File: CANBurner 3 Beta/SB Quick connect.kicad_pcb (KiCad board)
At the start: 2 copper layers, 33.8 x 30 mm, 9 parts

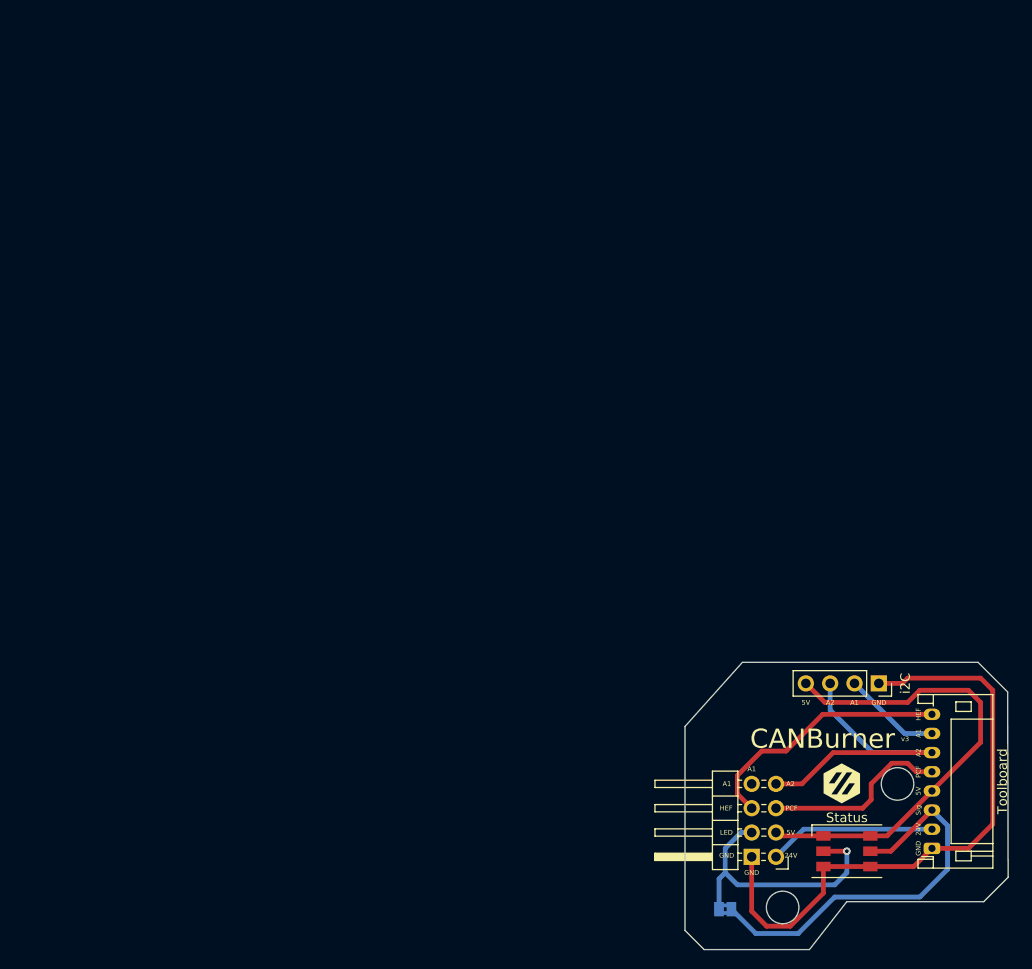
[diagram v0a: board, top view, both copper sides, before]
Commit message: Modified pin order on i2c header
Now fits better with the order most breakouts use.
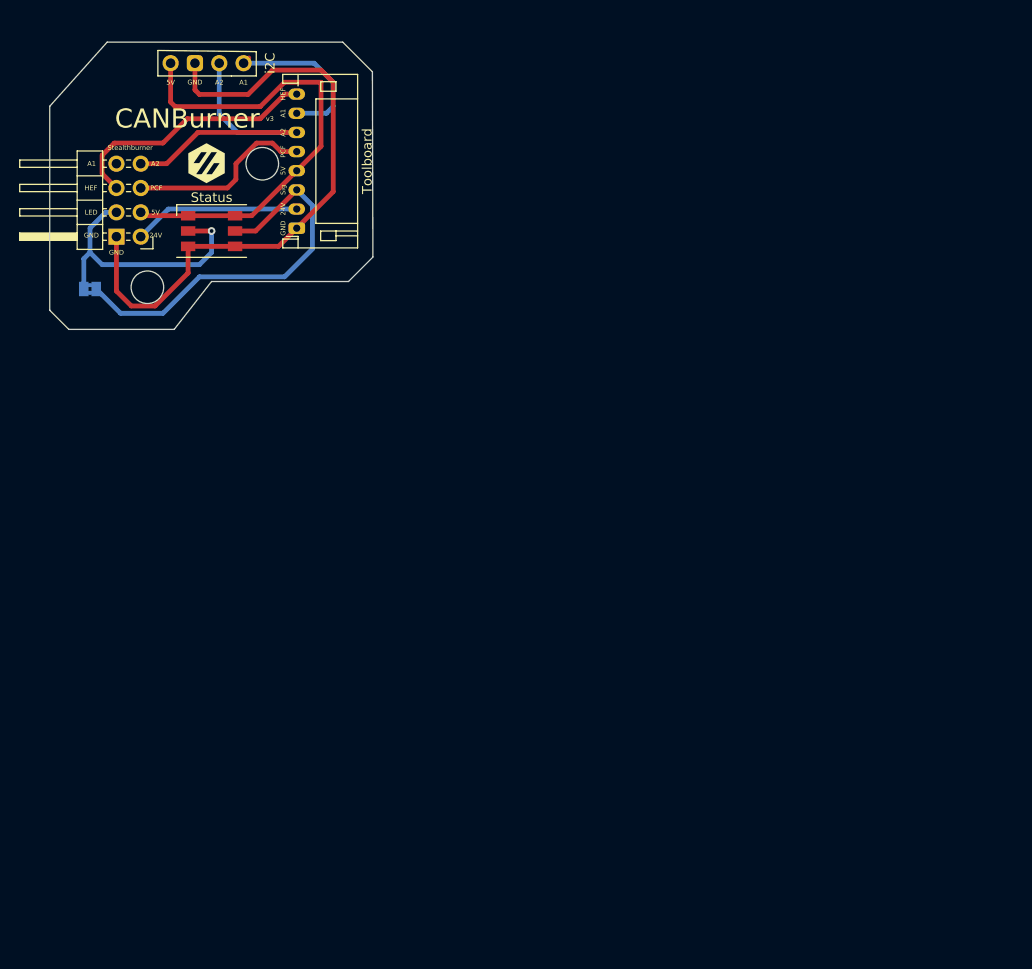
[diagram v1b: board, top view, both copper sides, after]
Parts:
- moved G*** 92.7 mm to (59.4, 29.2)
- moved LED Bypass 92.7 mm to (59.4, 48.3)
- moved Status 92.7 mm to (72.1, 42.2)
- moved G*** 92.7 mm to (71.6, 35.1) (x2)
- moved G*** 92.7 mm to (61.9, 26.7)
- moved Stealthburner 92.7 mm to (54.1, 35.2)
- moved Toolboard 92.7 mm to (81.0, 41.9)
- moved i2C 92.7 mm to (75.4, 24.7)
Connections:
- i2C pad 1: /GND -> /A1
- i2C pad 2: /A1 -> /A2
- i2C pad 3: /A2 -> /GND
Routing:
- net /A1: track 10.3 -> 17.6 mm
- net /A2: track 32.9 -> 31.8 mm
- net /GND: track 65.0 -> 66.0 mm
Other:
- outline, holes or cut-outs redrawn

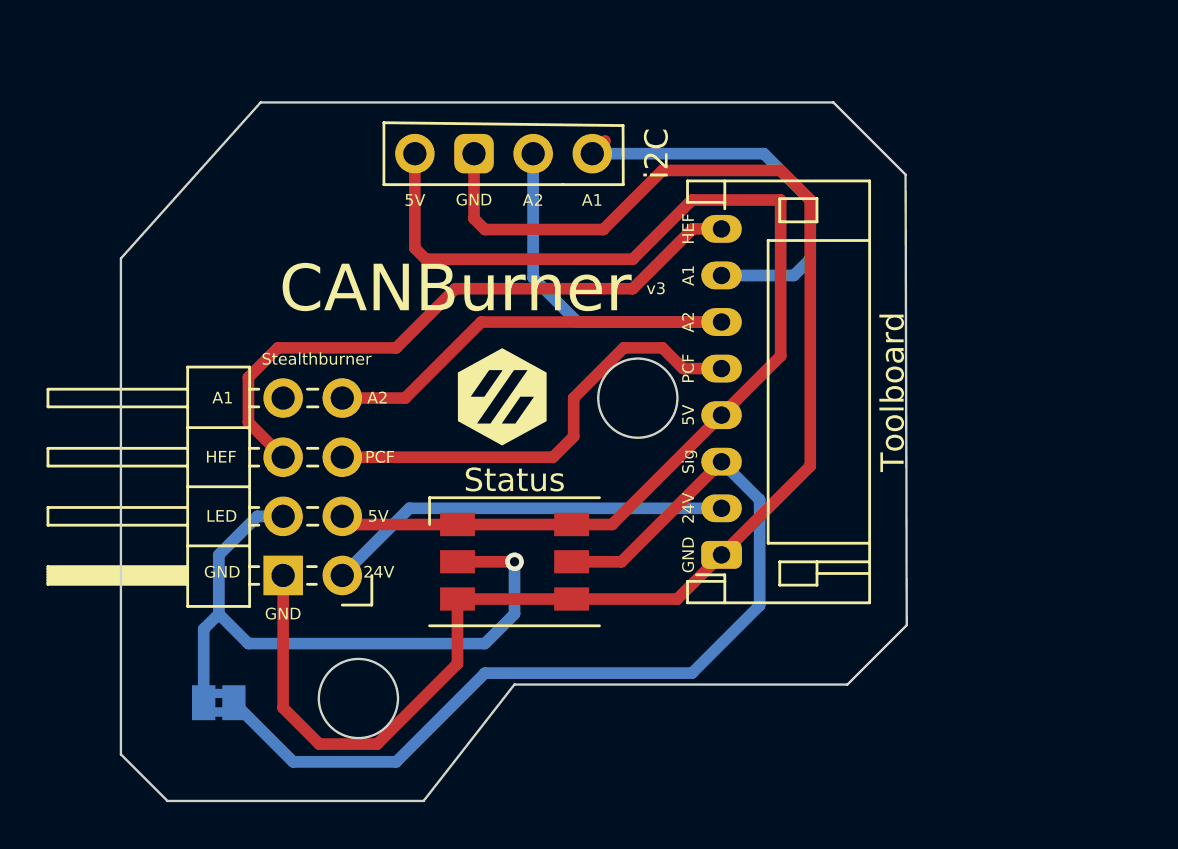
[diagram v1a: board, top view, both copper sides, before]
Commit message: Minor adjustments to LED Signal tracks
Moved tracks further from edges/mounting screws
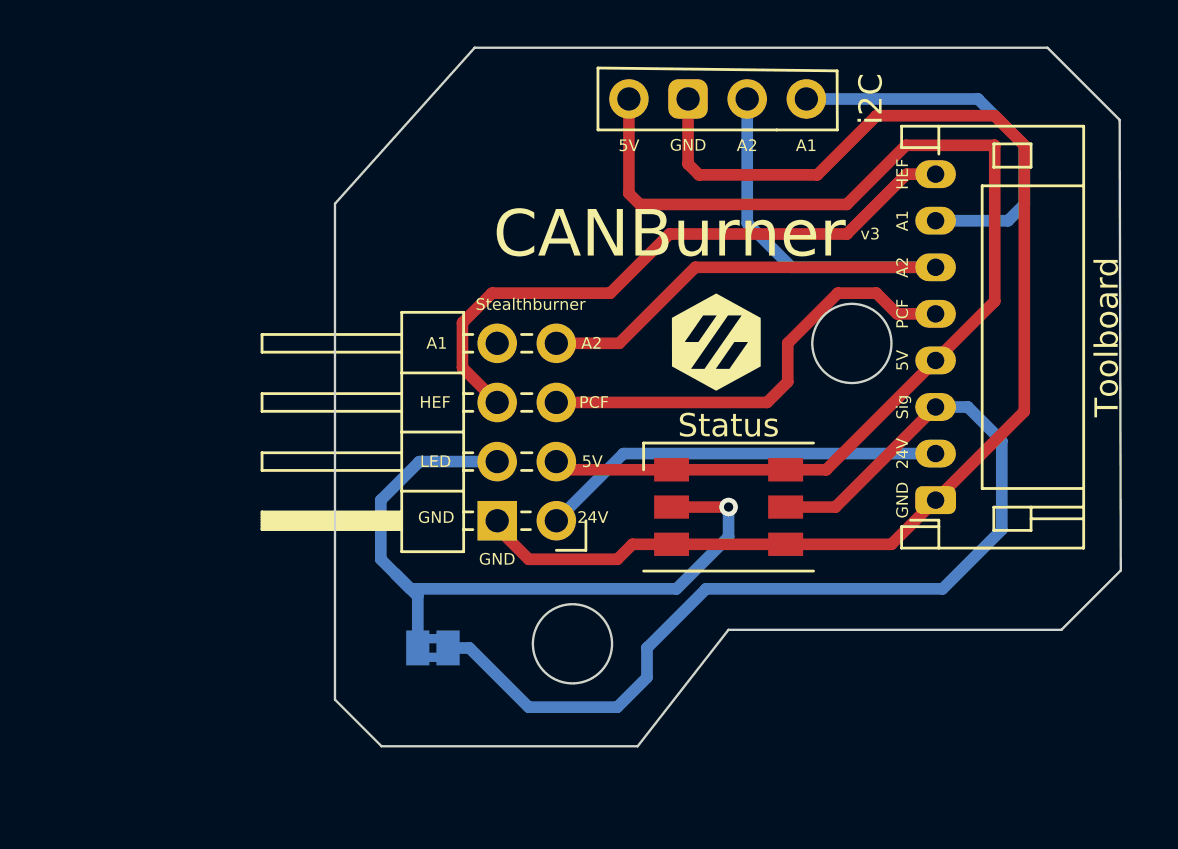
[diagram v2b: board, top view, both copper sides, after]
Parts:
- moved G*** 9.49 mm to (68.6, 26.9)
- moved G*** 9.49 mm to (80.8, 32.7) (x2)
- moved G*** 9.49 mm to (71.1, 24.3)
- moved LED Bypass 9.49 mm to (68.6, 45.9)
- moved Status 9.49 mm to (81.3, 39.9)
- moved Stealthburner 9.49 mm to (63.3, 32.8)
- moved Toolboard 9.49 mm to (90.2, 39.6)
- moved i2C 9.49 mm to (84.6, 22.3)
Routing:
- net /GND: track 66.0 -> 56.6 mm
- net /Sig: track 70.0 -> 76.1 mm
- net /A1: track 17.6 -> 16.8 mm

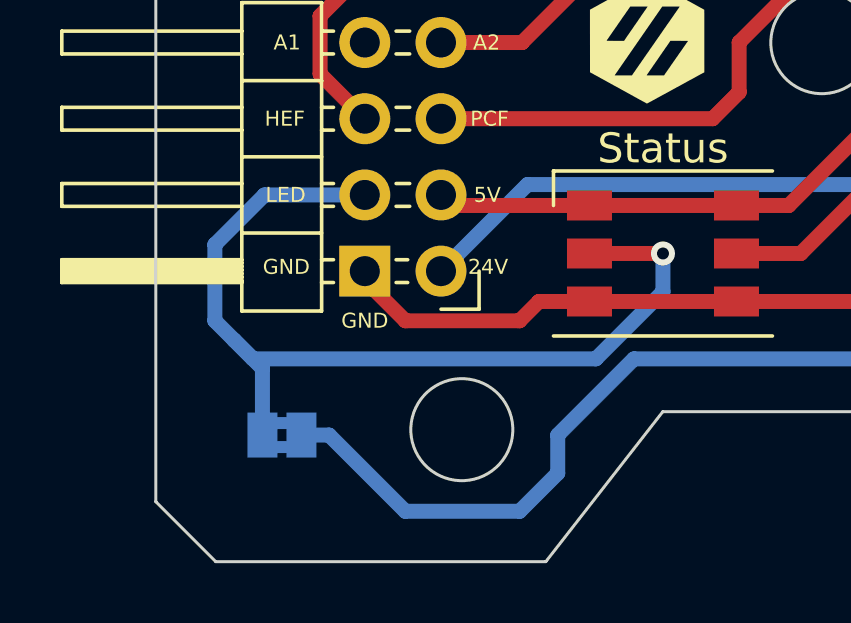
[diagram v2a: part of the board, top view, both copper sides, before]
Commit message: Another LED Signal Track tweak
Slightly adjusted the tracks on the bypass pad
so the path is more obvious when looking at tracks on printed board
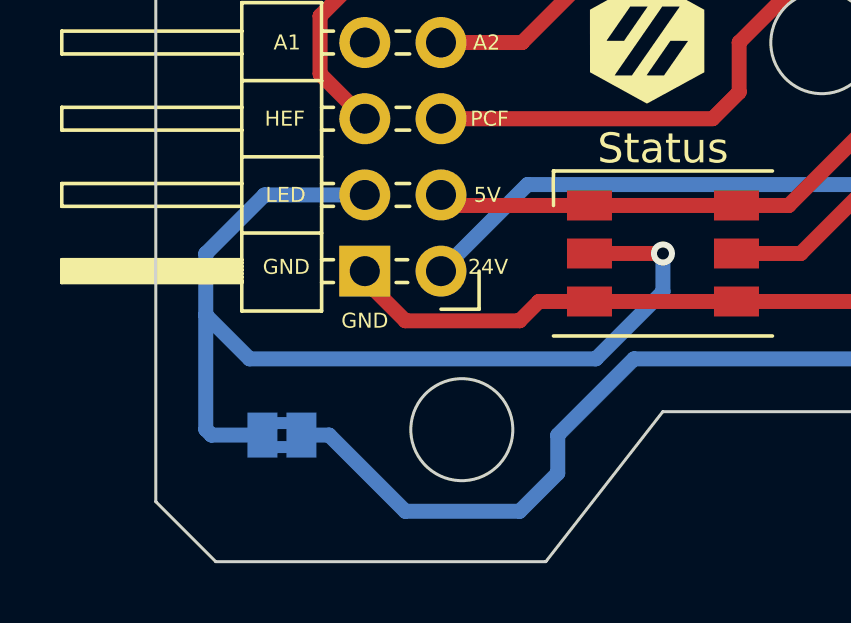
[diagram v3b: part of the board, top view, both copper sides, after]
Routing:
- net /Sig: track 76.1 -> 78.6 mm
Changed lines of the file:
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@@
   (segment (start 85.873186 39.856814) (end 83.73 39.856814) (width 0.5) (layer "F.Cu") (net 6))
   (via blind (at 81.28 39.856814) (size 0.8) (drill 0.4) (layers "F.Cu" "B.Cu") (free) (net 6))
-  (segment (start 81.28 39.856814) (end 81.28 41.133145) (width 0.5) (layer "B.Cu") (net 6))
   (segment (start 81.28 41.133145) (end 79.043145 43.37) (width 0.5) (layer "B.Cu") (net 6))
   (segment (start 93.013145 37.02) (end 93.013145 40.83) (width 0.5) (layer "B.Cu") (net 6))
   (segment (start 77.773145 45.91) (end 77.773145 47.18) (width 0.5) (layer "B.Cu") (net 6))
-  (segment (start 66.343145 42.1) (end 66.343145 39.56) (width 0.5) (layer "B.Cu") (net 6))
-  (segment (start 66.978145 42.735) (end 66.343145 42.1) (width 0.5) (layer "B.Cu") (net 6))
   (segment (start 91.553145 35.56) (end 93.013145 37.02) (width 0.5) (layer "B.Cu") (net 6))
-  (segment (start 67.93 45.91) (end 67.93 43.686855) (width 0.5) (layer "B.Cu") (net 6))
+  (segment (start 67.998119 37.905026) (end 71.341315 37.905026) (width 0.5) (layer "B.Cu") (net 6))
+  (segment (start 66.04 41.91) (end 66.04 39.863145) (width 0.5) (layer "B.Cu") (net 6))
   (segment (start 90.473145 43.37) (end 80.313145 43.37) (width 0.5) (layer "B.Cu") (net 6))
   (segment (start 90.17 35.56) (end 91.553145 35.56) (width 0.5) (layer "B.Cu") (net 6))
-  (segment (start 67.613145 43.37) (end 66.978145 42.735) (width 0.5) (layer "B.Cu") (net 6))
+  (segment (start 81.28 39.856814) (end 81.28 41.133145) (width 0.5) (layer "B.Cu") (net 6))
+  (segment (start 66.04 41.91) (end 66.04 45.72) (width 0.5) (layer "B.Cu") (net 6))
   (segment (start 70.153145 45.91) (end 69.23 45.91) (width 0.5) (layer "B.Cu") (net 6))
   (segment (start 72.693145 48.45) (end 70.153145 45.91) (width 0.5) (layer "B.Cu") (net 6))
   (segment (start 77.773145 47.18) (end 76.503145 48.45) (width 0.5) (layer "B.Cu") (net 6))
+  (segment (start 66.04 45.72) (end 66.23 45.91) (width 0.5) (layer "B.Cu") (net 6))
   (segment (start 93.013145 40.83) (end 90.473145 43.37) (width 0.5) (layer "B.Cu") (net 6))
   (segment (start 76.503145 48.45) (end 72.693145 48.45) (width 0.5) (layer "B.Cu") (net 6))
-  (segment (start 66.343145 39.56) (end 67.998119 37.905026) (width 0.5) (layer "B.Cu") (net 6))
-  (segment (start 67.998119 37.905026) (end 71.341315 37.905026) (width 0.5) (layer "B.Cu") (net 6))
+  (segment (start 67.5 43.37) (end 66.04 41.91) (width 0.5) (layer "B.Cu") (net 6))
   (segment (start 80.313145 43.37) (end 77.773145 45.91) (width 0.5) (layer "B.Cu") (net 6))
-  (segment (start 67.93 43.686855) (end 66.978145 42.735) (width 0.5) (layer "B.Cu") (net 6))
-  (segment (start 79.043145 43.37) (end 67.613145 43.37) (width 0.5) (layer "B.Cu") (net 6))
+  (segment (start 66.23 45.91) (end 67.93 45.91) (width 0.5) (layer "B.Cu") (net 6))
+  (segment (start 66.04 39.863145) (end 67.998119 37.905026) (width 0.5) (layer "B.Cu") (net 6))
+  (segment (start 79.043145 43.37) (end 67.5 43.37) (width 0.5) (layer "B.Cu") (net 6))
   (segment (start 74.233103 38.256814) (end 73.881315 37.905026) (width 0.5) (layer "F.Cu") (net 7))
   (segment (start 83.73 38.256814) (end 78.83 38.256814) (width 0.5) (layer "F.Cu") (net 7))
